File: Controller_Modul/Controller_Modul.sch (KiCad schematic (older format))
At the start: 136 parts, among them J101 Screw_Terminal_01x06, J102 Conn_02x01, J103 Conn_01x06_Male, J104 Conn_02x01, J105 Conn_01x04_Male, J106 Conn_01x08_Male, J107 Micro_SD_Card_Det, J108 Conn_02x07_Odd_Even, J109 Conn_02x20_Odd_Even, J110 USB_B_Mini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

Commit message: Controller Modul geroutet
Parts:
- removed J108: Conn_02x07_Odd_Even, Connector_PinHeader_2.54mm:PinHeader_2x07_P2.54mm_Vertical, symbol Connector_Generic:Conn_02x07_Odd_Even
- J106: footprint ProjectFootprints:ST7789_Waveshare -> ProjectFootprints:ST7789_Waveshare2; symbol Connector:Conn_01x08_Male -> Connector_Generic:Conn_02x08_Counter_Clockwise
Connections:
- net labels added: USB_FS_D+, USB_FS_D-
- net labels removed: PA11, PA12, USB_FS_DM, USB_FS_DP
- wire segments 442 -> 435
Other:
- note added: "TODO: Length Matching SDIO, SPI beachten\nConnector für Display mit CPU-Board abstimmen\nESD Schutz USB-Buchse\nStatus LED"
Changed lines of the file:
@@
 Text Label 2150 5250 2    50   ~ 0
 TIM1_CH1_Z
-Text Label 4300 3850 0    50   ~ 0
-PA11
 Text Label 4650 3850 0    50   ~ 0
-USB_FS_DM
+USB_FS_D-
 Text Label 4650 3950 0    50   ~ 0
-USB_FS_DP
-Text Label 4300 3950 0    50   ~ 0
-PA12
+USB_FS_D+
 Wire Wire Line
 	4650 3950 4300 3950
@@
 TIM8_ENC_CH2
 $Comp
-L Connector:Conn_01x08_Male J?
+L Connector_Generic:Conn_02x08_Counter_Clockwise J?
 U 1 1 61385E73
 P 9100 9350
@@
 F 0 "J106" H 9206 9828 50  0000 C CNN
 F 1 "Conn_01x08_Male" H 9206 9737 50  0000 C CNN
-F 2 "ProjectFootprints:ST7789_Waveshare" H 9100 9350 50  0001 C CNN
+F 2 "ProjectFootprints:ST7789_Waveshare2" H 9100 9350 50  0001 C CNN
 F 3 "~" H 9100 9350 50  0001 C CNN
 	1    9100 9350
-	-1   0    0    -1
+	1    0    0    -1
 $EndComp
 $Comp
@@
 	8450 3700 8250 3700
 Text Label 8250 3600 2    50   ~ 0
-USB_FS_DM
+USB_FS_D+
 Wire Wire Line
 	8450 3600 8250 3600
 Text Label 8250 3700 2    50   ~ 0
-USB_FS_DP
+USB_FS_D-
 $Comp
 L power:PWR_FLAG #FLG0102
@@
 	1    0    0    -1
 $EndComp
-$Comp
-L Connector_Generic:Conn_02x07_Odd_Even J108
-U 1 1 605095AE
-P 6150 9500
-F 0 "J108" H 6200 10017 50  0000 C CNN
-F 1 "Conn_02x07_Odd_Even" H 6200 9926 50  0000 C CNN
-F 2 "Connector_PinHeader_2.54mm:PinHeader_2x07_P2.54mm_Vertical" H 6150 9500 50  0001 C CNN
-F 3 "~" H 6150 9500 50  0001 C CNN
-	1    6150 9500
-	1    0    0    -1
-$EndComp
-$Comp
-L power:+3V3 #PWR?
-U 1 1 60509B6F
-P 5550 9200
-AR Path="/5FDD0F66/60509B6F" Ref="#PWR?"  Part="1"
-AR Path="/60509B6F" Ref="#PWR0174"  Part="1"
-F 0 "#PWR0174" H 5550 9050 50  0001 C CNN
-F 1 "+3V3" H 5565 9373 50  0000 C CNN
-F 2 "" H 5550 9200 50  0001 C CNN
-F 3 "" H 5550 9200 50  0001 C CNN
-	1    5550 9200
-	1    0    0    -1
-$EndComp
-$Comp
-L power:GND #PWR?
-U 1 1 60509DE1
-P 6800 9200
-AR Path="/5FDD0F66/60509DE1" Ref="#PWR?"  Part="1"
-AR Path="/60509DE1" Ref="#PWR0175"  Part="1"
-F 0 "#PWR0175" H 6800 8950 50  0001 C CNN
-F 1 "GND" V 6805 9072 50  0000 R CNN
-F 2 "" H 6800 9200 50  0001 C CNN
-F 3 "" H 6800 9200 50  0001 C CNN
-	1    6800 9200
-	0    -1   -1   0
-$EndComp
-Wire Wire Line
-	5950 9200 5550 9200
-Text Label 5550 9300 2    50   ~ 0
-DISP_DIN
-Text Label 6850 9300 0    50   ~ 0
-DISP_CLK
-Text Label 5550 9400 2    50   ~ 0
-DISP_CS
-Text Label 6850 9400 0    50   ~ 0
-DISP_DC
-Text Label 5550 9500 2    50   ~ 0
-DISP_RST
-Text Label 6850 9500 0    50   ~ 0
-DISP_RST
-Text Label 5550 9600 2    50   ~ 0
-DISP_BL
-Text Label 5550 9700 2    50   ~ 0
+Text Label 9800 9050 0    50   ~ 0
 TIM8_ENC_CH2
-Text Label 5550 9800 2    50   ~ 0
+Text Label 9800 9150 0    50   ~ 0
 TIM8_ENC_CH1
-Text Label 6850 9800 0    50   ~ 0
+Text Label 9800 9250 0    50   ~ 0
 ENC_BTN
-$Comp
-L power:GND #PWR?
-U 1 1 6057FCD9
-P 6800 9600
-AR Path="/5FDD0F66/6057FCD9" Ref="#PWR?"  Part="1"
-AR Path="/6057FCD9" Ref="#PWR0176"  Part="1"
-F 0 "#PWR0176" H 6800 9350 50  0001 C CNN
-F 1 "GND" V 6805 9472 50  0000 R CNN
-F 2 "" H 6800 9600 50  0001 C CNN
-F 3 "" H 6800 9600 50  0001 C CNN
-	1    6800 9600
-	0    -1   -1   0
-$EndComp
-Wire Wire Line
-	6450 9600 6450 9700
-Connection ~ 6450 9600
-Wire Wire Line
-	6850 9800 6450 9800
-Wire Wire Line
-	5950 9800 5550 9800
-Wire Wire Line
-	5550 9700 5950 9700
-Wire Wire Line
-	5950 9600 5550 9600
-Wire Wire Line
-	5550 9500 5950 9500
-Wire Wire Line
-	5950 9400 5550 9400
-Wire Wire Line
-	5550 9300 5950 9300
-Wire Wire Line
-	6850 9300 6450 9300
-Wire Wire Line
-	6450 9400 6850 9400
-Wire Wire Line
-	6850 9500 6450 9500
-Wire Wire Line
-	6450 9200 6800 9200
-Wire Wire Line
-	6450 9600 6800 9600
+Wire Wire Line
+	9800 9250 9400 9250
+Wire Wire Line
+	9400 9150 9800 9150
+Wire Wire Line
+	9800 9050 9400 9050
 $Comp
 L Device:C_Small C?
@@
 Wire Wire Line
 	11300 2050 11300 2400
+$Comp
+L power:GND #PWR?
+U 1 1 602E120E
+P 9400 9350
+AR Path="/5FDD0F66/602E120E" Ref="#PWR?"  Part="1"
+AR Path="/602E120E" Ref="#PWR0174"  Part="1"
+F 0 "#PWR0174" H 9400 9100 50  0001 C CNN
+F 1 "GND" V 9405 9222 50  0000 R CNN
+F 2 "" H 9400 9350 50  0001 C CNN
+F 3 "" H 9400 9350 50  0001 C CNN
+	1    9400 9350
+	0    -1   -1   0
+$EndComp
+Wire Wire Line
+	9400 9750 9400 9650
+Connection ~ 9400 9350
+Connection ~ 9400 9450
+Wire Wire Line
+	9400 9450 9400 9350
+Connection ~ 9400 9550
+Wire Wire Line
+	9400 9550 9400 9450
+Connection ~ 9400 9650
+Wire Wire Line
+	9400 9650 9400 9550
+Text Notes 5350 6750 0    129  ~ 0
+TODO: Length Matching SDIO, SPI beachten\nConnector für Display mit CPU-Board abstimmen\nESD Schutz USB-Buchse\nStatus LED
 $EndSCHEMATC

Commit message: display modul fertig
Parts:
- added U105: SRV05-4, Package_TO_SOT_SMD:SOT-23-6, symbol Power_Protection:SRV05-4
- J106: symbol Connector_Generic:Conn_02x08_Counter_Clockwise -> Connector_Generic:Conn_02x08_Top_Bottom
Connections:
- no-connect marks 8 -> 10
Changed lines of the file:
@@
 TIM8_ENC_CH2
 $Comp
-L Connector_Generic:Conn_02x08_Counter_Clockwise J?
+L Connector_Generic:Conn_02x08_Top_Bottom J?
 U 1 1 61385E73
 P 9100 9350
@@
 Text Notes 5350 6750 0    129  ~ 0
 TODO: Length Matching SDIO, SPI beachten\nConnector für Display mit CPU-Board abstimmen\nESD Schutz USB-Buchse\nStatus LED
+$Comp
+L Power_Protection:SRV05-4 U105
+U 1 1 60285F2C
+P 6750 3650
+F 0 "U105" H 6200 4350 50  0000 C CNN
+F 1 "SRV05-4" H 6150 4250 50  0000 C CNN
+F 2 "Package_TO_SOT_SMD:SOT-23-6" H 7450 3200 50  0001 C CNN
+F 3 "http://www.onsemi.com/pub/Collateral/SRV05-4-D.PDF" H 6750 3650 50  0001 C CNN
+F 4 "C316033" H 6150 4150 50  0000 C CNN "LCSC"
+	1    6750 3650
+	1    0    0    -1
+$EndComp
+NoConn ~ 6250 3550
+NoConn ~ 6250 3750
+$Comp
+L power:GND #PWR?
+U 1 1 603DCDB2
+P 6750 4150
+AR Path="/5FDD0F66/603DCDB2" Ref="#PWR?"  Part="1"
+AR Path="/603DCDB2" Ref="#PWR0176"  Part="1"
+F 0 "#PWR0176" H 6750 3900 50  0001 C CNN
+F 1 "GND" H 6900 4100 50  0000 C CNN
+F 2 "" H 6750 4150 50  0001 C CNN
+F 3 "" H 6750 4150 50  0001 C CNN
+	1    6750 4150
+	1    0    0    -1
+$EndComp
+$Comp
+L power:+3V3 #PWR?
+U 1 1 603DE440
+P 6750 3150
+AR Path="/5FDD0F66/603DE440" Ref="#PWR?"  Part="1"
+AR Path="/603DE440" Ref="#PWR0175"  Part="1"
+F 0 "#PWR0175" H 6750 3000 50  0001 C CNN
+F 1 "+3V3" H 6765 3323 50  0000 C CNN
+F 2 "" H 6750 3150 50  0001 C CNN
+F 3 "" H 6750 3150 50  0001 C CNN
+	1    6750 3150
+	1    0    0    -1
+$EndComp
+Text Label 7250 3550 0    50   ~ 0
+USB_FS_D+
+Text Label 7250 3750 0    50   ~ 0
+USB_FS_D-
 $EndSCHEMATC

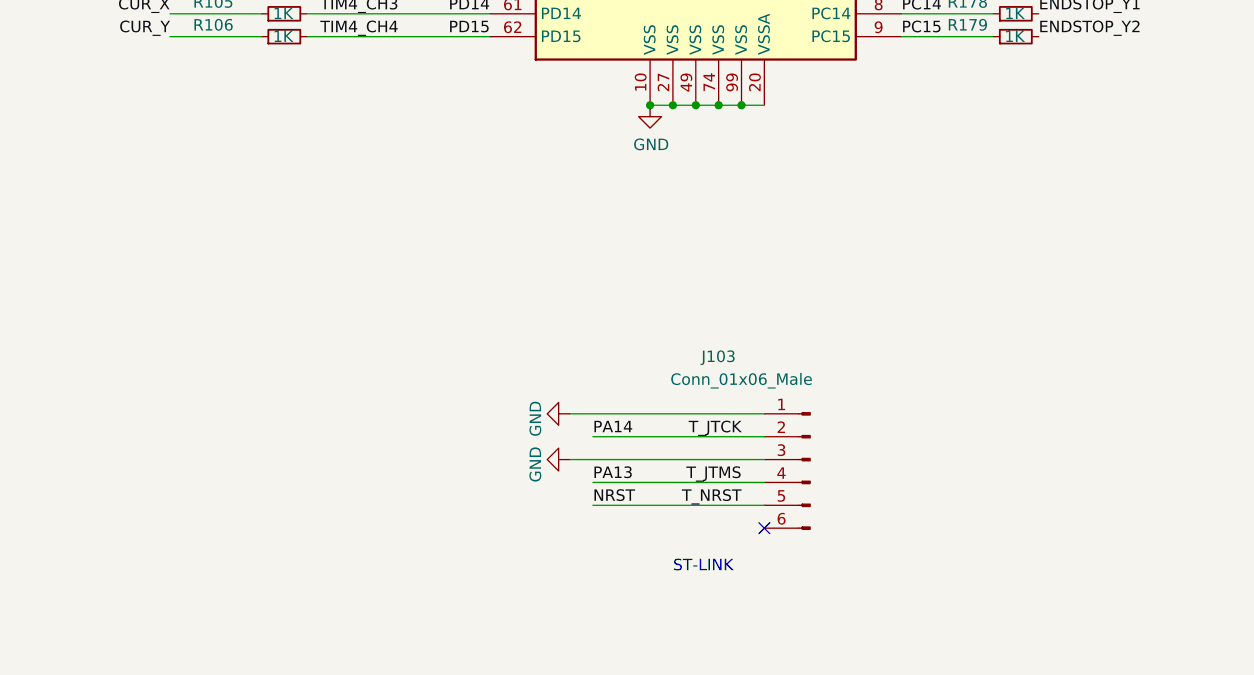
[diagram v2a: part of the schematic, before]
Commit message: Leere Symbole mit leeren Footprints hinzugefügt für BOM export
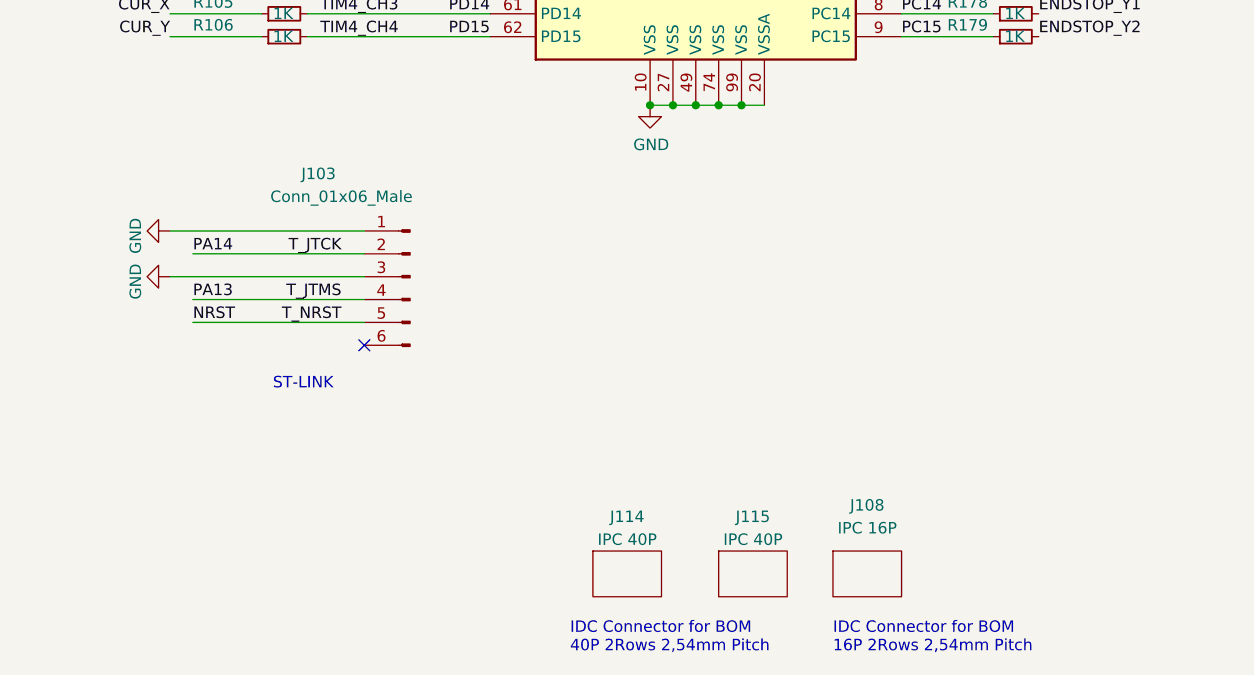
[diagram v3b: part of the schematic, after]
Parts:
- added J108: IPC 16P, ProjectFootprints:Empty, symbol PorjectLibrary:Empty
- added J114, J115: IPC 40P, ProjectFootprints:Empty, symbol PorjectLibrary:Empty
- J106: LCSC (none) -> C3406
- J109, J111: LCSC (none) -> C601944
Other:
- note added: "IDC Connector for BOM\n16P 2Rows 2,54mm Pitch"
- note added: "IDC Connector for BOM\n40P 2Rows 2,54mm Pitch"
- moved on the sheet: J103
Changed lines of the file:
@@
 L Connector:Conn_01x06_Male J?
 U 1 1 6006C002
-P 3900 9400
+P 2150 8600
 AR Path="/5FDD0F66/6006C002" Ref="J?"  Part="1"
 AR Path="/6006C002" Ref="J103"  Part="1"
-F 0 "J103" H 4300 9850 50  0000 C CNN
-F 1 "Conn_01x06_Male" H 4200 9750 50  0000 C CNN
-F 2 "Connector_PinHeader_2.54mm:PinHeader_1x06_P2.54mm_Vertical" H 3900 9400 50  0001 C CNN
-F 3 "~" H 3900 9400 50  0001 C CNN
-	1    3900 9400
+F 0 "J103" H 2550 9050 50  0000 C CNN
+F 1 "Conn_01x06_Male" H 2450 8950 50  0000 C CNN
+F 2 "Connector_PinHeader_2.54mm:PinHeader_1x06_P2.54mm_Vertical" H 2150 8600 50  0001 C CNN
+F 3 "~" H 2150 8600 50  0001 C CNN
+	1    2150 8600
 	-1   0    0    -1
 $EndComp
@@
 L power:GND #PWR?
 U 1 1 6006C009
-P 2850 9200
+P 1100 8400
 AR Path="/5FDD0F66/6006C009" Ref="#PWR?"  Part="1"
 AR Path="/6006C009" Ref="#PWR0123"  Part="1"
-F 0 "#PWR0123" H 2850 8950 50  0001 C CNN
-F 1 "GND" H 2950 9050 50  0000 R CNN
-F 2 "" H 2850 9200 50  0001 C CNN
-F 3 "" H 2850 9200 50  0001 C CNN
-	1    2850 9200
+F 0 "#PWR0123" H 1100 8150 50  0001 C CNN
+F 1 "GND" H 1200 8250 50  0000 R CNN
+F 2 "" H 1100 8400 50  0001 C CNN
+F 3 "" H 1100 8400 50  0001 C CNN
+	1    1100 8400
 	0    1    1    0
 $EndComp
 Wire Wire Line
-	3700 9200 2850 9200
-Text Label 3600 9300 2    50   ~ 0
+	1950 8400 1100 8400
+Text Label 1850 8500 2    50   ~ 0
 T_JTCK
 $Comp
 L power:GND #PWR?
 U 1 1 6006C011
-P 2850 9400
+P 1100 8600
 AR Path="/5FDD0F66/6006C011" Ref="#PWR?"  Part="1"
 AR Path="/6006C011" Ref="#PWR0124"  Part="1"
-F 0 "#PWR0124" H 2850 9150 50  0001 C CNN
-F 1 "GND" H 2950 9250 50  0000 R CNN
-F 2 "" H 2850 9400 50  0001 C CNN
-F 3 "" H 2850 9400 50  0001 C CNN
-	1    2850 9400
+F 0 "#PWR0124" H 1100 8350 50  0001 C CNN
+F 1 "GND" H 1200 8450 50  0000 R CNN
+F 2 "" H 1100 8600 50  0001 C CNN
+F 3 "" H 1100 8600 50  0001 C CNN
+	1    1100 8600
 	0    1    1    0
 $EndComp
-Text Label 3600 9500 2    50   ~ 0
+Text Label 1850 8700 2    50   ~ 0
 T_JTMS
-Text Label 3600 9600 2    50   ~ 0
+Text Label 1850 8800 2    50   ~ 0
 T_NRST
 Wire Wire Line
-	3700 9400 2850 9400
-Text Label 2950 9600 0    50   ~ 0
+	1950 8600 1100 8600
+Text Label 1200 8800 0    50   ~ 0
 NRST
 Wire Wire Line
-	2950 9600 3700 9600
-Text Label 2950 9500 0    50   ~ 0
+	1200 8800 1950 8800
+Text Label 1200 8700 0    50   ~ 0
 PA13
 Wire Wire Line
-	2950 9500 3700 9500
-Text Label 2950 9300 0    50   ~ 0
+	1200 8700 1950 8700
+Text Label 1200 8500 0    50   ~ 0
 PA14
 Wire Wire Line
-	2950 9300 3700 9300
-Text Notes 3300 9900 0    50   ~ 0
+	1200 8500 1950 8500
+Text Notes 1550 9100 0    50   ~ 0
 ST-LINK
-NoConn ~ 3700 9700
+NoConn ~ 1950 8900
 Text Label 4300 4150 0    50   ~ 0
 PA14
@@
 F 2 "Connector_PinHeader_2.54mm:PinHeader_2x20_P2.54mm_Vertical" H 14050 5950 50  0001 C CNN
 F 3 "~" H 14050 5950 50  0001 C CNN
+F 4 "C601944" H 14050 5950 50  0001 C CNN "LCSC"
 	1    14050 5950
 	1    0    0    -1
@@
 F 2 "ProjectFootprints:ST7789_Waveshare2" H 9100 9350 50  0001 C CNN
 F 3 "~" H 9100 9350 50  0001 C CNN
+F 4 "C3406" H 9100 9350 50  0001 C CNN "LCSC"
 	1    9100 9350
 	1    0    0    -1
@@
 F 2 "Connector_PinHeader_2.54mm:PinHeader_2x20_P2.54mm_Vertical" H 11050 5950 50  0001 C CNN
 F 3 "~" H 11050 5950 50  0001 C CNN
+F 4 "C601944" H 11050 5950 50  0001 C CNN "LCSC"
 	1    11050 5950
 	1    0    0    -1
@@
 Text Label 7250 3750 0    50   ~ 0
 USB_FS_D-
+$Comp
+L PorjectLibrary:Empty J108
+U 1 1 6029D132
+P 4150 9900
+F 0 "J108" H 4150 10200 50  0000 C CNN
+F 1 "IPC 16P" H 4150 10100 50  0000 C CNN
+F 2 "ProjectFootprints:Empty" H 4150 9900 50  0001 C CNN
+F 3 "~" H 4150 9900 50  0001 C CNN
+F 4 "C8372" H 4150 9900 50  0001 C CNN "LCSC"
+	1    4150 9900
+	1    0    0    -1
+$EndComp
+Text Notes 4000 10250 0    50   ~ 0
+IDC Connector for BOM\n16P 2Rows 2,54mm Pitch
+$Comp
+L PorjectLibrary:Empty J114
+U 1 1 6026697E
+P 3100 9900
+F 0 "J114" H 3100 10150 50  0000 C CNN
+F 1 "IPC 40P" H 3100 10050 50  0000 C CNN
+F 2 "ProjectFootprints:Empty" H 3100 9900 50  0001 C CNN
+F 3 "~" H 3100 9900 50  0001 C CNN
+F 4 "C601933" H 3100 9900 50  0001 C CNN "LCSC"
+	1    3100 9900
+	1    0    0    -1
+$EndComp
+$Comp
+L PorjectLibrary:Empty J115
+U 1 1 60DA27AD
+P 3650 9900
+F 0 "J115" H 3650 10150 50  0000 C CNN
+F 1 "IPC 40P" H 3650 10050 50  0000 C CNN
+F 2 "ProjectFootprints:Empty" H 3650 9900 50  0001 C CNN
+F 3 "~" H 3650 9900 50  0001 C CNN
+F 4 "C601933" H 3650 9900 50  0001 C CNN "LCSC"
+	1    3650 9900
+	1    0    0    -1
+$EndComp
+Text Notes 2850 10250 0    50   ~ 0
+IDC Connector for BOM\n40P 2Rows 2,54mm Pitch
 $EndSCHEMATC

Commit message: BOM für LCSC überarbeitet. Tool für BOM export modifiziert
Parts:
- C108: LCSC C696854 -> C1849
- H101, H102, H103, H104, J103, J105, L102, L103, R102, SW101, U101: LCSC (none) -> 0
- J102, J104: LCSC (none) -> C358684
- J110: LCSC (none) -> C46392
- R180, R181: LCSC C99198 -> 0
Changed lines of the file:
@@
 F 2 "Connector_PinHeader_2.54mm:PinHeader_1x02_P2.54mm_Vertical" H 7150 1100 50  0001 C CNN
 F 3 "~" H 7150 1100 50  0001 C CNN
+F 4 "C358684" H 7150 1100 50  0001 C CNN "LCSC"
 	1    7150 1100
 	1    0    0    -1
@@
 F 2 "Connector_PinHeader_2.54mm:PinHeader_1x02_P2.54mm_Vertical" H 2900 1000 50  0001 C CNN
 F 3 "~" H 2900 1000 50  0001 C CNN
+F 4 "C358684" H 2900 1000 50  0001 C CNN "LCSC"
 	1    2900 1000
 	1    0    0    -1
@@
 F 2 "Resistor_SMD:R_0603_1608Metric" H 1600 2950 50  0001 C CNN
 F 3 "~" H 1600 2950 50  0001 C CNN
+F 4 "0" H 1600 2950 50  0001 C CNN "LCSC"
 	1    1600 2950
 	0    1    1    0
@@
 F 2 "Connector_PinHeader_2.54mm:PinHeader_1x06_P2.54mm_Vertical" H 2150 8600 50  0001 C CNN
 F 3 "~" H 2150 8600 50  0001 C CNN
+F 4 "0" H 2150 8600 50  0001 C CNN "LCSC"
 	1    2150 8600
 	-1   0    0    -1
@@
 F 2 "Capacitor_SMD:C_1210_3225Metric" H 3950 2200 50  0001 C CNN
 F 3 "~" H 3950 2200 50  0001 C CNN
-F 4 " C696854 " H 3950 2200 50  0001 C CNN "LCSC"
+F 4 "C1849" H 3950 2200 50  0001 C CNN "LCSC"
 	1    3950 2200
 	1    0    0    -1
@@
 F 2 "ProjectFootprints:L_CommonModeChoke_Coilcraft_1812CAN" H 12150 1750 50  0001 C CNN
 F 3 "~" H 12150 1750 50  0001 C CNN
+F 4 "0" H 12150 1750 50  0001 C CNN "LCSC"
 	1    12150 1750
 	1    0    0    -1
@@
 F 2 "Package_QFP:LQFP-100_14x14mm_P0.5mm" H 2700 2650 50  0001 R CNN
 F 3 "http://www.st.com/st-web-ui/static/active/en/resource/technical/document/datasheet/DM00141306.pdf" H 3400 5150 50  0001 C CNN
+F 4 "0" H 3400 5150 50  0001 C CNN "LCSC"
 	1    3400 5150
 	1    0    0    -1
@@
 F 2 "ProjectFootprints:L_CommonModeChoke_Coilcraft_1812CAN" H 12150 3600 50  0001 C CNN
 F 3 "~" H 12150 3600 50  0001 C CNN
+F 4 "0" H 12150 3600 50  0001 C CNN "LCSC"
 	1    12150 3600
 	1    0    0    -1
@@
 F 2 "Rotary_Encoder:RotaryEncoder_Alps_EC11E-Switch_Vertical_H20mm_CircularMountingHoles" H 8450 8010 50  0001 C CNN
 F 3 "~" H 8600 8110 50  0001 C CNN
+F 4 "0" H 8600 7850 50  0001 C CNN "LCSC"
 	1    8600 7850
 	1    0    0    -1
@@
 F 2 "Connector_PinHeader_2.54mm:PinHeader_1x04_P2.54mm_Vertical" H 8850 2500 50  0001 C CNN
 F 3 "~" H 8850 2500 50  0001 C CNN
+F 4 "0" H 8850 2500 50  0001 C CNN "LCSC"
 	1    8850 2500
 	-1   0    0    -1
@@
 F 2 "Connector_USB:USB_B_OST_USB-B1HSxx_Horizontal" H 8900 3550 50  0001 C CNN
 F 3 "~" H 8900 3550 50  0001 C CNN
+F 4 "C46392" H 8750 3600 50  0001 C CNN "LCSC"
 	1    8750 3600
 	-1   0    0    -1
@@
 F 2 "MountingHole:MountingHole_3.2mm_M3_Pad_Via" H 7700 4750 50  0001 C CNN
 F 3 "~" H 7700 4750 50  0001 C CNN
+F 4 "0" H 7700 4750 50  0001 C CNN "LCSC"
 	1    7700 4750
 	0    1    1    0
@@
 F 2 "MountingHole:MountingHole_3.2mm_M3_Pad_Via" H 7700 4950 50  0001 C CNN
 F 3 "~" H 7700 4950 50  0001 C CNN
+F 4 "0" H 7700 4950 50  0001 C CNN "LCSC"
 	1    7700 4950
 	0    1    1    0
@@
 F 2 "MountingHole:MountingHole_3.2mm_M3_Pad_Via" H 7700 5150 50  0001 C CNN
 F 3 "~" H 7700 5150 50  0001 C CNN
+F 4 "0" H 7700 5150 50  0001 C CNN "LCSC"
 	1    7700 5150
 	0    1    1    0
@@
 F 2 "MountingHole:MountingHole_3.2mm_M3_Pad_Via" H 7700 5350 50  0001 C CNN
 F 3 "~" H 7700 5350 50  0001 C CNN
+F 4 "0" H 7700 5350 50  0001 C CNN "LCSC"
 	1    7700 5350
 	0    1    1    0
@@
 F 2 "Resistor_SMD:R_0603_1608Metric" H 10250 1850 50  0001 C CNN
 F 3 "~" H 10250 1850 50  0001 C CNN
-F 4 "C99198" H 10250 1850 50  0001 C CNN "LCSC"
+F 4 "0" H 10250 1850 50  0001 C CNN "LCSC"
 	1    10250 1850
 	0    -1   -1   0
@@
 F 2 "Resistor_SMD:R_0603_1608Metric" H 10250 3700 50  0001 C CNN
 F 3 "~" H 10250 3700 50  0001 C CNN
-F 4 "C99198" H 10250 3700 50  0001 C CNN "LCSC"
+F 4 "0" H 10250 3700 50  0001 C CNN "LCSC"
 	1    10250 3700
 	0    -1   -1   0

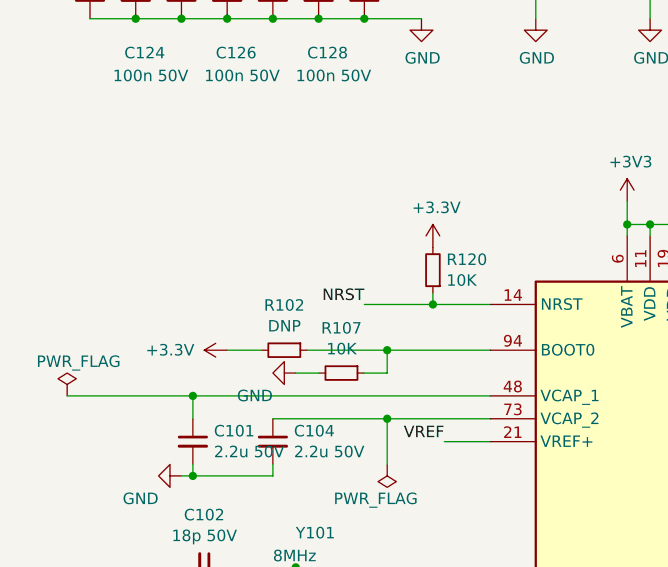
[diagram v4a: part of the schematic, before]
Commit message: CV Modul Reset Button hinzugefügt
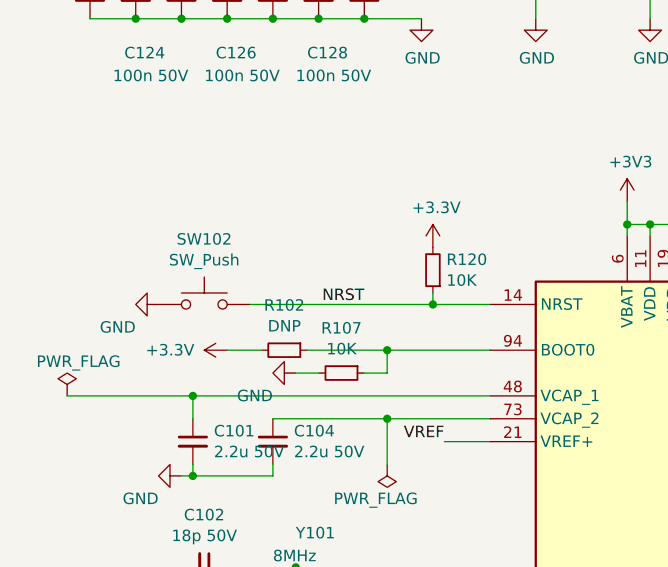
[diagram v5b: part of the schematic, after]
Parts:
- added SW102: SW_Push, ProjectFootprints:TactileSwitchLCSC, symbol Switch:SW_Push
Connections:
- net GND: now also SW102.1
- net NRST: now also SW102.2
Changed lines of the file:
@@
 Wire Wire Line
 	2250 2750 2250 2700
-Wire Wire Line
-	1950 2750 2250 2750
 Connection ~ 2250 2750
 Text Label 1950 2750 2    50   ~ 0
@@
 Text Notes 2850 10250 0    50   ~ 0
 IDC Connector for BOM\n40P 2Rows 2,54mm Pitch
+$Comp
+L Switch:SW_Push SW102
+U 1 1 602ADDB2
+P 1250 2750
+F 0 "SW102" H 1250 3035 50  0000 C CNN
+F 1 "SW_Push" H 1250 2944 50  0000 C CNN
+F 2 "ProjectFootprints:TactileSwitchLCSC" H 1250 2950 50  0001 C CNN
+F 3 "" H 1250 2950 50  0001 C CNN
+F 4 "C455137" H -1650 -3100 50  0001 C CNN "LCSC"
+	1    1250 2750
+	1    0    0    -1
+$EndComp
+$Comp
+L power:GND #PWR?
+U 1 1 602ADDB8
+P 1050 2750
+AR Path="/5FDD0F66/602ADDB8" Ref="#PWR?"  Part="1"
+AR Path="/602ADDB8" Ref="#PWR0180"  Part="1"
+F 0 "#PWR0180" H 1050 2500 50  0001 C CNN
+F 1 "GND" V 1150 2650 50  0000 R CNN
+F 2 "" H 1050 2750 50  0001 C CNN
+F 3 "" H 1050 2750 50  0001 C CNN
+	1    1050 2750
+	0    1    1    0
+$EndComp
+Wire Wire Line
+	1450 2750 2250 2750
 $EndSCHEMATC
